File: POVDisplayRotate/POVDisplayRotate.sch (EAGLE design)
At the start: 48 parts, among them U1 STP08DP05, U2 STP08DP05, U3 MPQ4420Q, U4 CY8CKIT-142, U5 M95M01

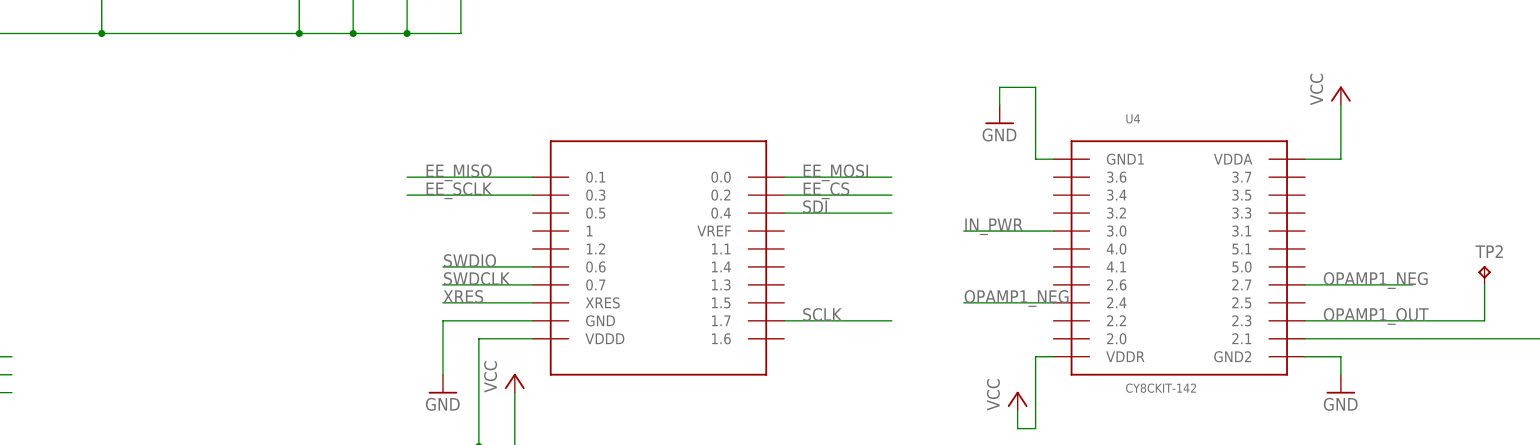
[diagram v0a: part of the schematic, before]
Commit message: Moved EEP to get more room
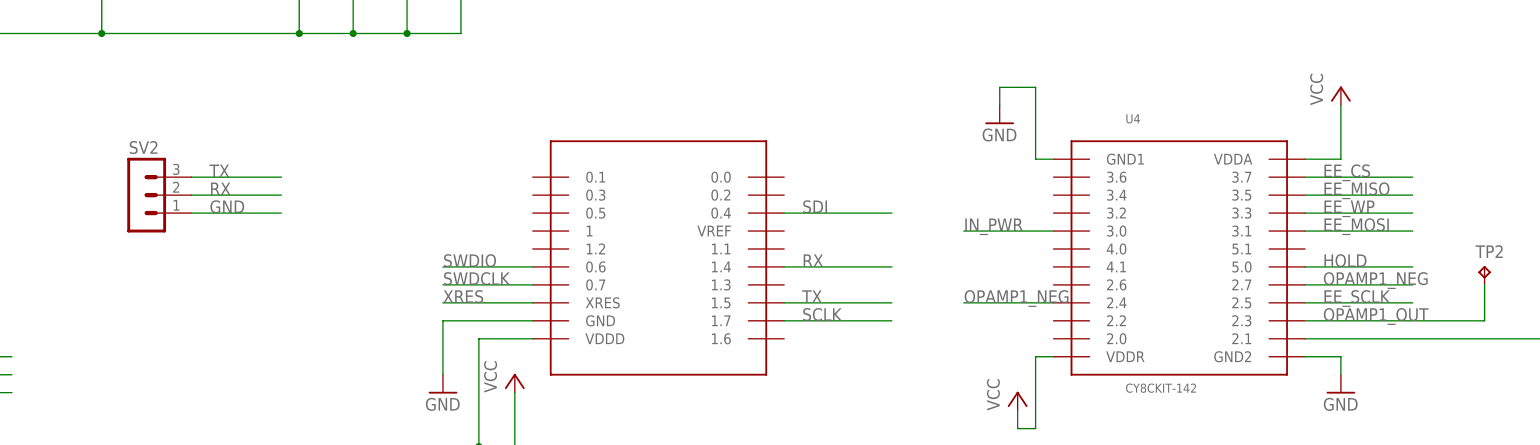
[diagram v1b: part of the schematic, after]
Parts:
- added SV2: (no value), con-lstb:MA03-1
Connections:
- new net HOLD: U4.5.0
- new net RX: SV2.2, U4.1.4
- new net TX: SV2.3, U4.1.5
- net EE_CS: now also U4.3.7; no longer U4.0.2
- net EE_MISO: now also U4.3.5; no longer U4.0.1
- net EE_MOSI: now also U4.3.1; no longer U4.0.0
- net EE_SCLK: now also U4.2.5; no longer U4.0.3
- net EE_WP: now also U4.3.3
- net GND: now also SV2.1
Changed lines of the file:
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@@
 <part name="GND3" library="supply1" deviceset="GND" device=""/>
 <part name="GND5" library="supply1" deviceset="GND" device=""/>
+<part name="SV2" library="con-lstb" deviceset="MA03-1" device=""/>
 </parts>
 <sheets>
@@
 <instance part="GND3" gate="1" x="147.32" y="53.34"/>
 <instance part="GND5" gate="1" x="276.86" y="68.58"/>
+<instance part="SV2" gate="G$1" x="193.04" y="35.56"/>
 </instances>
 <busses>
@@
 <pinref part="GND5" gate="1" pin="GND"/>
 </segment>
+<segment>
+<pinref part="SV2" gate="G$1" pin="1"/>
+<wire x1="200.66" y1="33.02" x2="213.36" y2="33.02" width="0.1524" layer="91"/>
+<label x="203.2" y="33.02" size="1.778" layer="95"/>
+</segment>
 </net>
 <net name="EE_MISO" class="0">
@@
 </segment>
 <segment>
-<pinref part="U4" gate="G$1" pin="0.1"/>
-<wire x1="248.92" y1="38.1" x2="231.14" y2="38.1" width="0.1524" layer="91"/>
-<label x="233.68" y="38.1" size="1.778" layer="95"/>
+<pinref part="U4" gate="G$1" pin="3.5"/>
+<wire x1="358.14" y1="35.56" x2="373.38" y2="35.56" width="0.1524" layer="91"/>
+<label x="360.68" y="35.56" size="1.778" layer="95"/>
 </segment>
 </net>
@@
 </segment>
 <segment>
-<pinref part="U4" gate="G$1" pin="0.0"/>
-<wire x1="284.48" y1="38.1" x2="299.72" y2="38.1" width="0.1524" layer="91"/>
-<label x="287.02" y="38.1" size="1.778" layer="95"/>
+<pinref part="U4" gate="G$1" pin="3.1"/>
+<wire x1="358.14" y1="30.48" x2="373.38" y2="30.48" width="0.1524" layer="91"/>
+<label x="360.68" y="30.48" size="1.778" layer="95"/>
 </segment>
 </net>
@@
 </segment>
 <segment>
-<pinref part="U4" gate="G$1" pin="0.2"/>
-<wire x1="284.48" y1="35.56" x2="299.72" y2="35.56" width="0.1524" layer="91"/>
-<label x="287.02" y="35.56" size="1.778" layer="95"/>
+<pinref part="U4" gate="G$1" pin="3.7"/>
+<wire x1="358.14" y1="38.1" x2="373.38" y2="38.1" width="0.1524" layer="91"/>
+<label x="360.68" y="38.1" size="1.778" layer="95"/>
 </segment>
 </net>
@@
 <label x="325.12" y="-30.48" size="1.778" layer="95"/>
 </segment>
+<segment>
+<pinref part="U4" gate="G$1" pin="3.3"/>
+<wire x1="358.14" y1="33.02" x2="373.38" y2="33.02" width="0.1524" layer="91"/>
+<label x="360.68" y="33.02" size="1.778" layer="95"/>
+</segment>
 </net>
 <net name="EE_HOLD" class="0">
@@
 </segment>
 <segment>
-<pinref part="U4" gate="G$1" pin="0.3"/>
-<wire x1="248.92" y1="35.56" x2="231.14" y2="35.56" width="0.1524" layer="91"/>
-<label x="233.68" y="35.56" size="1.778" layer="95"/>
+<pinref part="U4" gate="G$1" pin="2.5"/>
+<wire x1="358.14" y1="20.32" x2="373.38" y2="20.32" width="0.1524" layer="91"/>
+<label x="360.68" y="20.32" size="1.778" layer="95"/>
 </segment>
 </net>
@@
 </segment>
 </net>
+<net name="HOLD" class="0">
+<segment>
+<pinref part="U4" gate="G$1" pin="5.0"/>
+<wire x1="358.14" y1="25.4" x2="373.38" y2="25.4" width="0.1524" layer="91"/>
+<label x="360.68" y="25.4" size="1.778" layer="95"/>
+</segment>
+</net>
+<net name="TX" class="0">
+<segment>
+<pinref part="U4" gate="G$1" pin="1.5"/>
+<wire x1="284.48" y1="20.32" x2="299.72" y2="20.32" width="0.1524" layer="91"/>
+<label x="287.02" y="20.32" size="1.778" layer="95"/>
+</segment>
+<segment>
+<pinref part="SV2" gate="G$1" pin="3"/>
+<wire x1="200.66" y1="38.1" x2="213.36" y2="38.1" width="0.1524" layer="91"/>
+<label x="203.2" y="38.1" size="1.778" layer="95"/>
+</segment>
+</net>
+<net name="RX" class="0">
+<segment>
+<pinref part="U4" gate="G$1" pin="1.4"/>
+<wire x1="284.48" y1="25.4" x2="299.72" y2="25.4" width="0.1524" layer="91"/>
+<label x="287.02" y="25.4" size="1.778" layer="95"/>
+</segment>
+<segment>
+<pinref part="SV2" gate="G$1" pin="2"/>
+<wire x1="200.66" y1="35.56" x2="213.36" y2="35.56" width="0.1524" layer="91"/>
+<label x="203.2" y="35.56" size="1.778" layer="95"/>
+</segment>
+</net>

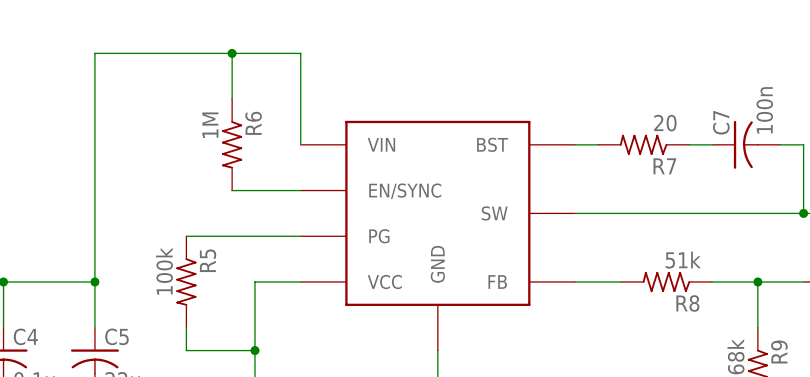
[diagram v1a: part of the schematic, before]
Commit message: Updated the library and POVDisplay board with part numbers.
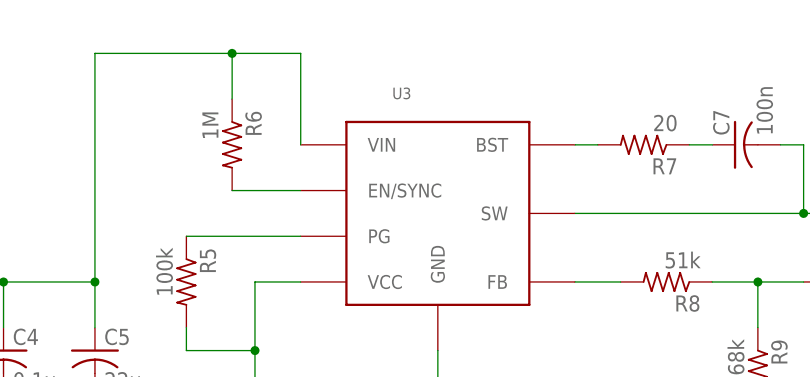
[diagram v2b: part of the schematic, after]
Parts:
- U1, U2: DIGIKEY (none) -> 497-6119-1-ND
- U3: DIGIKEY (none) -> 1589-1293-1-ND
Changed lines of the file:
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@@
 <grid distance="0.1" unitdist="inch" unit="inch" style="lines" multiple="1" display="no" altdistance="0.01" altunitdist="inch" altunit="inch"/>
 <layers>
-<layer number="1" name="Top" color="4" fill="1" visible="no" active="no"/>
-<layer number="16" name="Bottom" color="1" fill="1" visible="no" active="no"/>
-<layer number="17" name="Pads" color="2" fill="1" visible="no" active="no"/>
-<layer number="18" name="Vias" color="2" fill="1" visible="no" active="no"/>
-<layer number="19" name="Unrouted" color="6" fill="1" visible="no" active="no"/>
-<layer number="20" name="Dimension" color="15" fill="1" visible="no" active="no"/>
-<layer number="21" name="tPlace" color="16" fill="1" visible="no" active="no"/>
-<layer number="22" name="bPlace" color="14" fill="1" visible="no" active="no"/>
-<layer number="23" name="tOrigins" color="15" fill="1" visible="no" active="no"/>
-<layer number="24" name="bOrigins" color="15" fill="1" visible="no" active="no"/>
-<layer number="25" name="tNames" color="7" fill="1" visible="no" active="no"/>
-<layer number="26" name="bNames" color="7" fill="1" visible="no" active="no"/>
-<layer number="27" name="tValues" color="7" fill="1" visible="no" active="no"/>
-<layer number="28" name="bValues" color="7" fill="1" visible="no" active="no"/>
+<layer number="1" name="Top" color="4" fill="1" visible="yes" active="no"/>
+<layer number="16" name="Bottom" color="1" fill="1" visible="yes" active="no"/>
+<layer number="17" name="Pads" color="2" fill="1" visible="yes" active="no"/>
+<layer number="18" name="Vias" color="2" fill="1" visible="yes" active="no"/>
+<layer number="19" name="Unrouted" color="6" fill="1" visible="yes" active="no"/>
+<layer number="20" name="Dimension" color="15" fill="1" visible="yes" active="no"/>
+<layer number="21" name="tPlace" color="16" fill="1" visible="yes" active="no"/>
+<layer number="22" name="bPlace" color="14" fill="1" visible="yes" active="no"/>
+<layer number="23" name="tOrigins" color="15" fill="1" visible="yes" active="no"/>
+<layer number="24" name="bOrigins" color="15" fill="1" visible="yes" active="no"/>
+<layer number="25" name="tNames" color="7" fill="1" visible="yes" active="no"/>
+<layer number="26" name="bNames" color="7" fill="1" visible="yes" active="no"/>
+<layer number="27" name="tValues" color="7" fill="1" visible="yes" active="no"/>
+<layer number="28" name="bValues" color="7" fill="1" visible="yes" active="no"/>
 <layer number="29" name="tStop" color="7" fill="3" visible="no" active="no"/>
 <layer number="30" name="bStop" color="7" fill="6" visible="no" active="no"/>
@@
 <layer number="35" name="tGlue" color="7" fill="4" visible="no" active="no"/>
 <layer number="36" name="bGlue" color="7" fill="5" visible="no" active="no"/>
-<layer number="37" name="tTest" color="7" fill="1" visible="no" active="no"/>
-<layer number="38" name="bTest" color="7" fill="1" visible="no" active="no"/>
+<layer number="37" name="tTest" color="7" fill="1" visible="yes" active="no"/>
+<layer number="38" name="bTest" color="7" fill="1" visible="yes" active="no"/>
 <layer number="39" name="tKeepout" color="4" fill="11" visible="no" active="no"/>
 <layer number="40" name="bKeepout" color="1" fill="11" visible="no" active="no"/>
@@
 <layer number="44" name="Drills" color="7" fill="1" visible="no" active="no"/>
 <layer number="45" name="Holes" color="7" fill="1" visible="no" active="no"/>
-<layer number="46" name="Milling" color="3" fill="1" visible="no" active="no"/>
-<layer number="47" name="Measures" color="7" fill="1" visible="no" active="no"/>
-<layer number="48" name="Document" color="7" fill="1" visible="no" active="no"/>
-<layer number="49" name="Reference" color="7" fill="1" visible="no" active="no"/>
-<layer number="51" name="tDocu" color="6" fill="1" visible="no" active="no"/>
-<layer number="52" name="bDocu" color="7" fill="1" visible="no" active="no"/>
+<layer number="46" name="Milling" color="3" fill="1" visible="yes" active="no"/>
+<layer number="47" name="Measures" color="7" fill="1" visible="yes" active="no"/>
+<layer number="48" name="Document" color="7" fill="1" visible="yes" active="no"/>
+<layer number="49" name="Reference" color="7" fill="1" visible="yes" active="no"/>
+<layer number="51" name="tDocu" color="6" fill="1" visible="yes" active="no"/>
+<layer number="52" name="bDocu" color="7" fill="1" visible="yes" active="no"/>
 <layer number="90" name="Modules" color="5" fill="1" visible="yes" active="yes"/>
 <layer number="91" name="Nets" color="2" fill="1" visible="yes" active="yes"/>
@@
 <part name="C11" library="resistor" deviceset="C-US" device="C0603" value="1u"/>
 <part name="U4" library="NicksParts" deviceset="CY8CKIT-142" device=""/>
-<part name="U1" library="NicksParts" deviceset="STP08DP05" device=""/>
-<part name="U2" library="NicksParts" deviceset="STP08DP05" device=""/>
+<part name="U1" library="NicksParts" deviceset="STP08DP05" device="">
+<attribute name="DIGIKEY" value="497-6119-1-ND"/>
+</part>
+<part name="U2" library="NicksParts" deviceset="STP08DP05" device="">
+<attribute name="DIGIKEY" value="497-6119-1-ND"/>
+</part>
 <part name="P+5" library="supply1" deviceset="VCC" device=""/>
 <part name="P+2" library="supply1" deviceset="VCC" device=""/>
@@
 <attribute name="DIGIKEY" value="P0.0GCT-ND"/>
 </part>
-<part name="U3" library="NicksParts" deviceset="MPQ4420Q" device=""/>
+<part name="U3" library="NicksParts" deviceset="MPQ4420Q" device="">
+<attribute name="DIGIKEY" value="1589-1293-1-ND"/>
+</part>
 <part name="P+9" library="supply1" deviceset="VCC" device=""/>
 <part name="C6" library="resistor" deviceset="C-US" device="C0603" value="0.1u">
@@
 <instance part="C11" gate="G$1" x="238.76" y="71.12"/>
 <instance part="U4" gate="G$1" x="304.8" y="27.94"/>
-<instance part="U1" gate="G$1" x="58.42" y="-15.24"/>
-<instance part="U2" gate="G$1" x="129.54" y="-15.24"/>
+<instance part="U1" gate="G$1" x="58.42" y="-15.24">
+<attribute name="DIGIKEY" x="58.42" y="-15.24" size="1.778" layer="96" display="off"/>
+</instance>
+<instance part="U2" gate="G$1" x="129.54" y="-15.24">
+<attribute name="DIGIKEY" x="129.54" y="-15.24" size="1.778" layer="96" display="off"/>
+</instance>
 <instance part="P+5" gate="VCC" x="109.22" y="0"/>
 <instance part="P+2" gate="VCC" x="38.1" y="0"/>
@@
 <attribute name="DIGIKEY" x="101.6" y="-27.94" size="1.778" layer="96" rot="R270" display="off"/>
 </instance>
-<instance part="U3" gate="G$1" x="152.4" y="91.44"/>
+<instance part="U3" gate="G$1" x="152.4" y="91.44">
+<attribute name="DIGIKEY" x="152.4" y="91.44" size="1.778" layer="96" display="off"/>
+</instance>
 <instance part="P+9" gate="VCC" x="246.38" y="10.16"/>
 <instance part="C6" gate="G$1" x="132.08" y="68.58">
